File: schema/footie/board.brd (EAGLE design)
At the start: 78.4 x 81.3 mm, 35 parts, among them T1 2N3565, U1 ATMEGA328P-MU, U2 USD-SOCKETNEW, U3 HC_05, U4 MCP73831, U5 3.3 regulator, Y1 8MHZ

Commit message: complete the first pcb version
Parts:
- moved D1 15.5 mm to (27.9, 57.1)
- moved U$3 11.7 mm to (20.3, 55.9)
- moved EEPROM 8.89 mm to (33.0, 38.1)
- moved R2 8.89 mm to (59.7, 35.6)
- moved R3 8.89 mm to (22.9, 47.0)
- moved U$1 8.89 mm to (48.3, 44.5)
- moved R1 8.89 mm to (33.0, 41.9)
- moved T1 8.89 mm to (20.3, 41.9)
- moved C6 7.41 mm to (43.2, 25.4)
- moved U1 5.24 mm to (35.6, 22.9)
- moved LED1 4.58 mm to (47.0, 17.8)
- moved LED3 4.58 mm to (44.5, 17.8)
- moved U$4 3.81 mm to (38.1, 50.8)
- moved C3 2.84 mm to (59.7, 17.8)
- moved C4 2.54 mm to (54.6, 21.6)
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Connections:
- net GND renamed N$22
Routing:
- net +3V3: track 198.6 -> 287.4 mm, vias 8 -> 11
- net N$22: track 312.2 -> 369.8 mm, vias 16 -> 17
- net GPSRX: track 0.00 -> 53.7 mm, vias 0 -> 3
- net GPSTX: track 0.00 -> 49.8 mm, vias 0 -> 4
- net SD_MOSI: track 0.00 -> 36.6 mm, vias 0 -> 2
- net SD_SCK: track 0.95 -> 35.8 mm, vias 0 -> 4
- net D3: track 21.1 -> 44.4 mm, vias 2 -> 4
- net DTR: track 41.7 -> 63.2 mm, vias 4 -> 2
- net ARDUINO_RX: track 115.6 -> 134.7 mm, vias 10 -> 6
- net N$20: track 24.1 -> 43.2 mm
- net D5: track 62.8 -> 47.3 mm
- net D9: track 10.2 -> 25.5 mm
- net N$16: track 71.2 -> 85.7 mm
- net D6: track 10.7 -> 24.7 mm, vias 0 -> 2
- net SD_MISO: track 29.5 -> 40.7 mm, vias 3 -> 2
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- added copper zone on layer 1, net GND
- added copper zone on layer 16, net GND
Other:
- outline, holes or cut-outs redrawn
- board text added: "FOOTIE 1.0V"

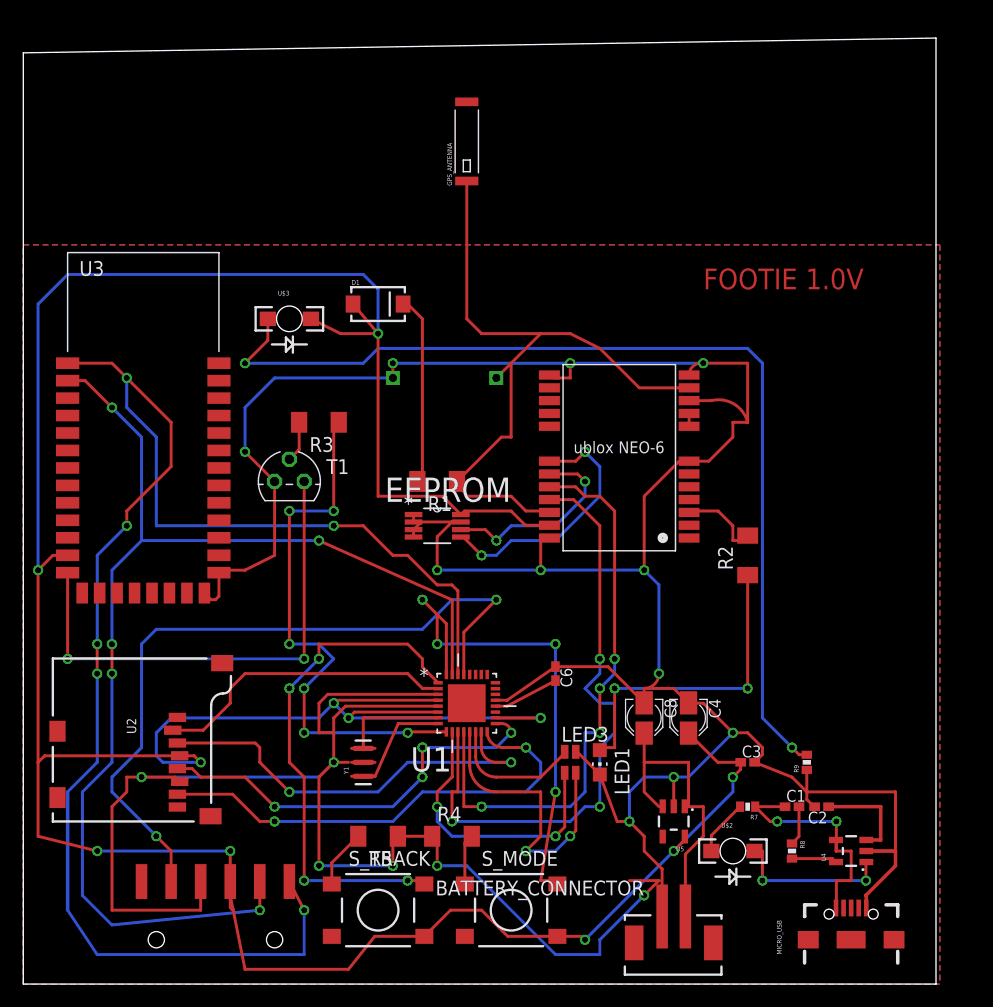
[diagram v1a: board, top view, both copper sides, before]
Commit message: update items to 1206 package update cpu update library
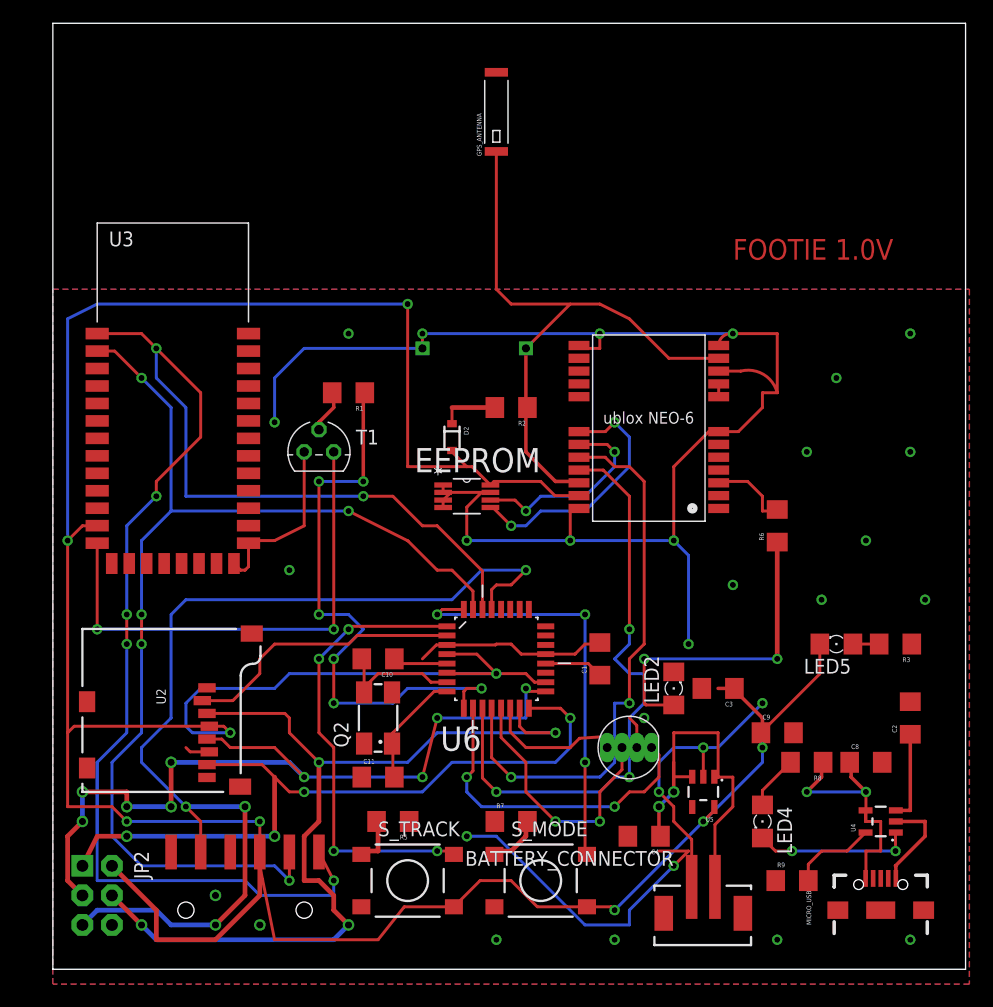
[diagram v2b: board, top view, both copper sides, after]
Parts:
- removed C6: 0.1 uF, resistor:C0402K
- removed LED1: (no value), led:CHIP-LED0805
- removed LED3: GM1WA55311A, led:GM1WA55311A
- removed R4: (no value), resistor:M1406
- removed U$2, U$3: HSMC-C265, SparkFun-Retired:HSMC-C265
- removed U1: ATMEGA328P-MU, Atmel_By_element14_Batch_1-00:QFN50P500X500X100-33N
- removed Y1: 8MHZ, SparkFun-FreqCtrl:RESONATOR-SMD
- added C10, C11: 22 uF, SparkFun-Capacitors:1206
- added C9: 4.7 uF, SparkFun-Capacitors:1206
- added D2: 250mA/100V, SparkFun-DiscreteSemi:SOD-323
- added JP2: AVR_SPI_PRG_6NS, SparkFun-Connectors:2X3-NS
- added LED2, LED4, LED5: (no value), eagle-ltspice:LED_1206
- added Q2: (no value), crystal:CTS406
- added R6: 1K, SparkFun-Passives:1206
- added U6: ATMEGA328P-AU, Ava:QFP80P900X900X120-32N
- C1: value 4.7 uF -> 0.1 uF; device resistor:C0402K -> SparkFun-Capacitors:1206
- C2: device resistor:C0402K -> SparkFun-Capacitors:1206
- C3: value 4.7 uF -> 10 uF; device resistor:C0402K -> SparkFun-Capacitors:1206
- C4: value 10 uf -> 10 uF; device resistor:PANASONIC_A -> SparkFun-Capacitors:1206
- C8: value 10 uf -> 4.7 uF; device resistor:PANASONIC_A -> SparkFun-Capacitors:1206
- D1: value (none) -> LED-RGB-CC-THRUCLEAR; device SparkFun-DiscreteSemi:SMA-DIODE -> SparkFun-LED:LED-RGB-THRU
- R1: value (none) -> 100 ohm; device resistor:M1406 -> SparkFun-Passives:1206
- R2, R5: value (none) -> 1K; device resistor:M1406 -> SparkFun-Passives:1206
- R3: value 100 ohm -> 10K; device resistor:M1406 -> SparkFun-Passives:1206
- R7: value 330 -> 1K; device SparkFun-Passives:0402-RES -> SparkFun-Passives:1206
- R8: value 2K -> 330; device SparkFun-Passives:0402-RES -> SparkFun-Passives:1206
- R9: value 10k -> 2K; device SparkFun-Passives:0402-RES -> SparkFun-Passives:1206
- moved R3 53.1 mm to (72.4, 27.9)
- moved D1 43.8 mm to (49.5, 19.1)
- moved R2 24.0 mm to (39.4, 48.3), turned to 180 degrees
- moved C1 20.8 mm to (47.0, 26.7), turned to 90 degrees
- moved R7 20.4 mm to (39.4, 12.7), turned to 0 degrees
- moved C8 19.4 mm to (69.8, 17.8), turned to 0 degrees
- moved C4 10.9 mm to (50.8, 11.4), turned to 180 degrees
- moved R1 10.8 mm to (25.4, 49.5)
- moved C2 10.8 mm to (73.7, 21.6), turned to 90 degrees
- moved R9 10.2 mm to (63.5, 7.62), turned to 0 degrees
- moved R8 7.73 mm to (64.8, 17.8), turned to 180 degrees
- moved C3 6.84 mm to (57.1, 24.1), turned to 180 degrees
- moved MICRO_USB 3.59 mm to (71.1, 5.08)
- moved T1 3.59 mm to (22.9, 44.5)
- moved U$4 3.59 mm to (40.6, 53.3)
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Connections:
- removed net N$13: U1.8, Y1.1
- removed net N$14: U1.7, Y1.3
- removed net N$17: C6.2, U1.20
- new net GND: BATTERY_CONNECTOR.GND, C1.2, C10.1, C11.1, C2.2, C3.2, C4.2, C8.2, C9.2, D1.2, EEPROM.1, EEPROM.2, EEPROM.3, EEPROM.4, EEPROM.7, JP1.3, JP2.6, LED2.C, MICRO_USB.GND1, R3.1, R5.1, R7.1, R9.1, T1.3, U$1.10_GND, U$1.12_GND, U$1.13_GND, U$1.24_GND, U$1.7_VDDUSB, U$4.GND, U2.6, U3.21, U3.22, U4.2, U5.2, U6.21, U6.3, U6.5
- new net N$27: C11.2, Q2.1, U6.8
- new net N$29: C10.2, Q2.3, U6.7
- net +3V3: now also C9.1, D2.A, JP2.2, LED5.C, U6.18, U6.4, U6.6; no longer C4.+, D1.A, U$3.C, U1.18, U1.4, U1.6
- net ARDUINO_RX: now also U6.30; no longer U1.30
- net ARDUINO_TX: now also U6.31; no longer U1.31
- net D10: now also D1.4, U6.14; no longer LED3.1, U1.14
- net D2: now also U6.32; no longer U1.32
- net D3: now also U6.1; no longer U1.1
- net D5: now also R1.1, U6.9; no longer R3.1, U1.9
- net D6: now also D1.1, U6.10; no longer LED3.2, U1.10
- net D9: now also D1.3, U6.13; no longer LED3.3, U1.13
- net DTR: now also JP2.5, U6.29; no longer U1.29
- net GPSRX: now also U6.11; no longer U1.11
- net GPSTX: now also U6.12; no longer U1.12
- net N$1: now also D2.C, R2.2; no longer D1.C, R1.2
- net N$11: now also LED4.C; no longer U$2.C
- net N$12: now also C4.1; no longer C8.+
- net N$15: now also R9.2; no longer R8.2
- net N$16: now also LED5.A, R3.2; no longer R9.2, U$3.A
- net N$19: now also R1.2; no longer R3.2
- net N$2: now also C8.1, R8.1; no longer C1.1, R7.1
- net N$22: now also C1.1, U6.20; no longer BATTERY_CONNECTOR.GND, C1.2, C2.2, C3.2, C4.-, C6.1, C8.-, EEPROM.1, EEPROM.2, EEPROM.3, EEPROM.4, EEPROM.7, JP1.3, LED1.C, LED3.4, MICRO_USB.GND1, R4.1, R5.1, R8.1, R9.1, T1.3, U$1.10_GND, U$1.12_GND, U$1.13_GND, U$1.24_GND, U$1.7_VDDUSB, U$4.GND, U1.21, U1.3, U1.5, U2.6, U3.21, U3.22, U4.2, U5.2, Y1.2
- net N$3: now also R6.2; no longer R2.2
- net N$4: now also LED2.A, R6.1; no longer LED1.A, R2.1
- net N$6: now also R2.1; no longer R1.1
- net N$8: now also LED4.A, R8.2; no longer R7.2, U$2.A
- net N$9: now also R7.2; no longer R4.2
- net SD_CS: now also U6.2; no longer U1.2
- net SD_MISO: now also JP2.1, U6.16; no longer U1.16
- net SD_MOSI: now also JP2.4, U6.15; no longer U1.15
- net SD_SCK: now also JP2.3, U6.17; no longer U1.17
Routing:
- net N$22: track 369.8 -> 5.06 mm, vias 17 -> 0
- net GND: track 0.00 -> 230.0 mm, vias 0 -> 30
- net N$16: track 85.7 -> 2.41 mm, vias 2 -> 0
- net SD_MOSI: track 36.6 -> 77.6 mm, vias 2 -> 4
- net SD_SCK: track 35.8 -> 71.7 mm, vias 4 -> 9
- net DTR: track 63.2 -> 89.7 mm, vias 2 -> 4
- net SD_MISO: track 40.7 -> 63.4 mm, vias 2 -> 4
- net N$29: track 0.00 -> 11.4 mm
- net N$1: track 16.3 -> 5.07 mm
- net N$27: track 0.00 -> 10.1 mm
- net N$14: track 9.05 -> 0.00 mm
- net N$13: track 8.37 -> 0.00 mm
- net ARDUINO_RX: track 134.7 -> 126.7 mm
- net N$6: track 27.6 -> 20.0 mm
- net ARDUINO_TX: track 102.8 -> 96.5 mm
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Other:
- outline, holes or cut-outs redrawn
